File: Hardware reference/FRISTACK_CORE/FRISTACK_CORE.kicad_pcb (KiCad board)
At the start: 2 copper layers, 50 x 50 mm, 76 parts, among them J1 USB_C_Receptacle_USB2.0_16P, J3 Conn_01x04_Pin, J4 Conn_01x09_Socket, J5 Conn_01x12_Socket, J6 Conn_01x12_Socket, J7 Conn_01x04_Pin, J8 Conn_01x02_Pin, U1 AZ1117-3.3, U2 USBLC6-2SC6, U3 ESP32-S3-MINI-1U, U4 SN65HVD232, Y1 32.768 kHz

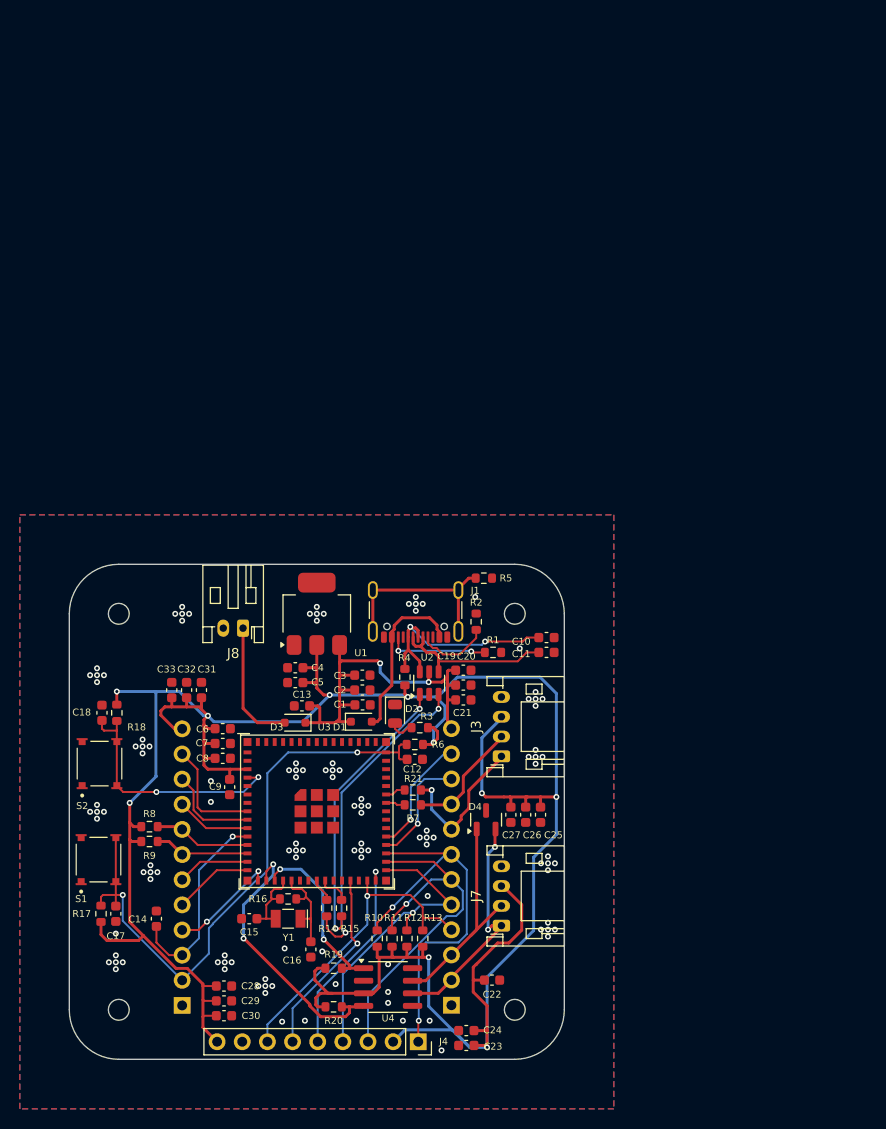
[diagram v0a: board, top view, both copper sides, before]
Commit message: Updated CORE schematic and PCB design
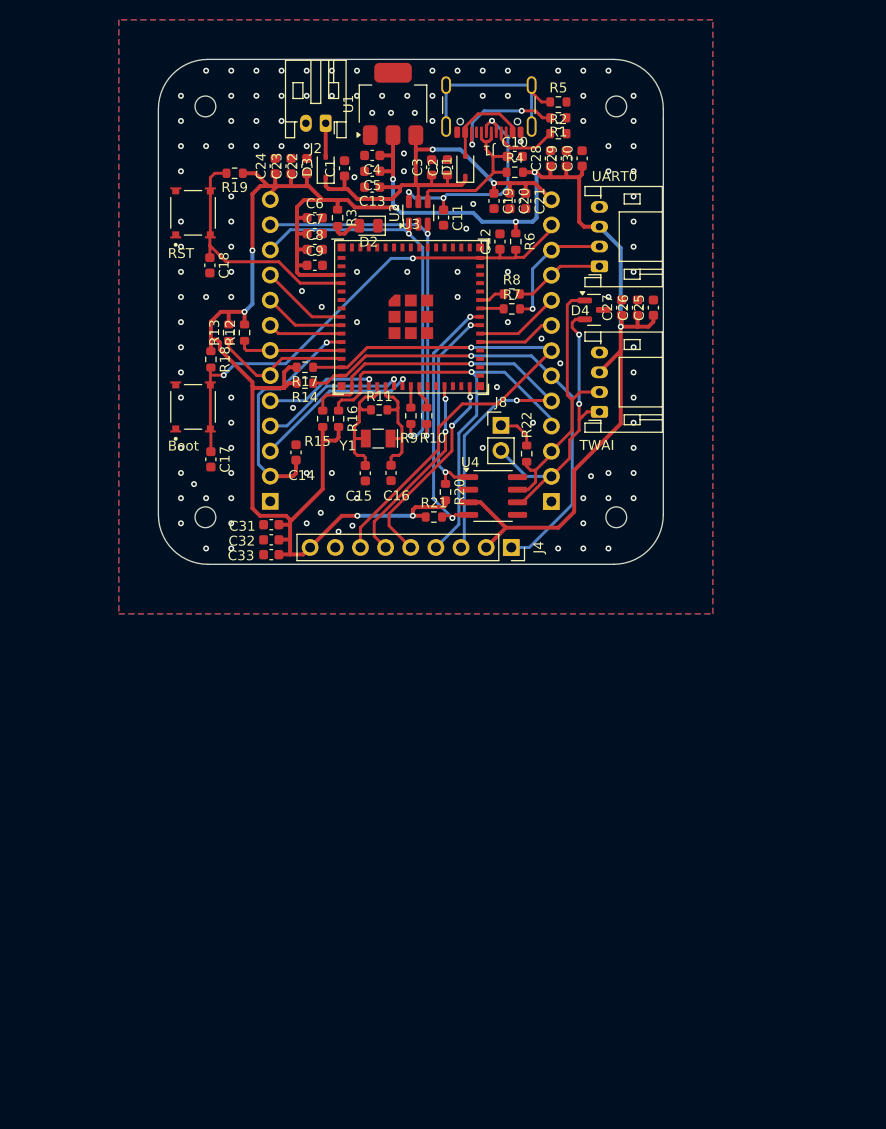
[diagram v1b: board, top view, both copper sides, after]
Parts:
- removed J3, J7: Conn_01x04_Pin, Connector_JST:JST_PH_S4B-PH-K_1x04_P2.00mm_Horizontal
- removed the REF** at (105.0, 105.0)
- removed the REF** at (105.0, 145.0)
- removed the REF** at (145.0, 145.0)
- removed the REF** at (145.0, 105.0)
- removed S1, S2: TL3315NF100Q, User_imports:SW_TL3315NF100Q
- added Boot: TL3315NF100Q, User_imports:SW_TL3315NF100Q, F.Cu at (112.5, 84.1)
- added J2: Conn_01x02_Pin, Connector_JST:JST_PH_S2B-PH-K_1x02_P2.00mm_Horizontal, F.Cu at (125.9, 55.5)
- added R22: 120, Resistor_SMD:R_0603_1608Metric, F.Cu at (146.2, 88.8)
- added REF**: MountingHole_2.1mm, MountingHole:MountingHole_2.1mm, F.Cu at (113.8, 95.2)
- added REF**: MountingHole_2.1mm, MountingHole:MountingHole_2.1mm, F.Cu at (155.2, 95.2)
- added REF**: MountingHole_2.1mm, MountingHole:MountingHole_2.1mm, F.Cu at (155.2, 53.8)
- added REF**: MountingHole_2.1mm, MountingHole:MountingHole_2.1mm, F.Cu at (113.8, 53.8)
- added RST: TL3315NF100Q, User_imports:SW_TL3315NF100Q, F.Cu at (112.5, 64.5)
- added TWAI: Conn_01x04_Pin, Connector_JST:JST_PH_S4B-PH-K_1x04_P2.00mm_Horizontal, F.Cu at (153.6, 84.6)
- added UART0: Conn_01x04_Pin, Connector_JST:JST_PH_S4B-PH-K_1x04_P2.00mm_Horizontal, F.Cu at (153.6, 69.9)
- J5, J6: value Conn_01x12_Socket -> Conn_01x13_Socket; footprint Connector_PinSocket_2.54mm:PinSocket_1x12_P2.54mm_Vertical -> Connector_PinSocket_2.54mm:PinSocket_1x13_P2.54mm_Vertical
- J8: footprint Connector_JST:JST_PH_S2B-PH-K_1x02_P2.00mm_Horizontal -> Connector_PinHeader_2.54mm:PinHeader_1x02_P2.54mm_Vertical
- R10: value 10K -> 0
- R11: value 10K -> ?
- R12, R13: value 10K -> 2K2
- R14, R15: value 0 -> 10K
- R16: value ? -> 10K
- R19: value 4K7 -> 10K
- R21: value 0 -> 4K7
- R8, R9: value 2K2 -> 0
- moved C30 93.9 mm to (151.8, 59.0), turned to 90 degrees
- moved C29 91.9 mm to (150.2, 59.0), turned to 90 degrees
- moved C23 90.6 mm to (122.4, 59.8), turned to 90 degrees
- moved C28 89.9 mm to (148.6, 59.0), turned to 90 degrees
- moved C24 89.4 mm to (120.8, 59.8), turned to 90 degrees
- moved C22 84.3 mm to (124.0, 59.8), turned to 90 degrees
- moved R19 80.9 mm to (116.7, 60.5)
- moved R8 65.1 mm to (144.7, 72.7), turned to 0 degrees
- moved R13 64.3 mm to (116.1, 76.6), turned to 90 degrees
- moved R12 63.4 mm to (117.7, 76.6), turned to 90 degrees
- moved R17 58.9 mm to (123.8, 80.1), turned to 180 degrees
- moved D1 57.1 mm to (140.0, 59.8), turned to 90 degrees
- moved D3 56.2 mm to (125.9, 59.9), turned to 90 degrees
- moved R1 54.4 mm to (149.4, 54.9)
- moved C1 54.2 mm to (127.8, 60.0), turned to 90 degrees
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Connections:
- J5 pad 10: I2S_DIN -> I2S_LRCK
- J5 pad 11: I2S_LRCK -> USB_DN_2
- J5 pad 12: ESP_PWR -> USB_DP_2
- J5 pad 2: EN -> ADC_1
- J5 pad 3: ADC_1 -> GPIO18
- J5 pad 4: GPIO12 -> GPIO17
- J5 pad 5: GPIO11 -> GPIO14
- J5 pad 6: GPIO10 -> SCL
- J5 pad 7: SCL -> SDA
- J5 pad 8: SDA -> I2S_DOUT
- J5 pad 9: I2S_DOUT -> I2S_DIN
- J6 pad 10: GPIO38 -> UART0_RX
- J6 pad 11: GPIO39 -> UART0_TX
- J6 pad 12: +5V -> EN
- J6 pad 4: CS -> MOSI
- J6 pad 5: MOSI -> SCK
- J6 pad 6: SCK -> MISO
- J6 pad 7: MISO -> CS
- J6 pad 8: UART0_RX -> GPIO39
- J6 pad 9: UART0_TX -> GPIO40
- J8 pad 1: Net-(D3-A) -> Net-(J8-Pin_1)
- J8 pad 2: GND -> CAN_L
- R10 pad 1: MISO -> Net-(U3-USB_D+)
- R10 pad 2: ESP_PWR -> USB_DP_2
- R11 pad 1: SCK -> X_TAL_N
- R11 pad 2: ESP_PWR -> X_TAL_P
- R12 pad 1: MOSI -> SDA
- R13 pad 1: CS -> SCL
- R14 pad 1: Net-(U3-USB_D-) -> MISO
- R14 pad 2: USB_DN_2 -> ESP_PWR
- R15 pad 1: Net-(U3-USB_D+) -> SCK
- R15 pad 2: USB_DP_2 -> ESP_PWR
- R16 pad 1: X_TAL_N -> MOSI
- R16 pad 2: X_TAL_P -> ESP_PWR
- R17 pad 1: ESP_PWR -> CS
- R17 pad 2: EN -> ESP_PWR
- R18 pad 2: GPIO0 -> EN
- R19 pad 1: CAN_D -> ESP_PWR
- R19 pad 2: ESP_PWR -> GPIO0
- R20 pad 1: ESP_PWR -> CAN_D
- R20 pad 2: CAN_R -> ESP_PWR
- R21 pad 1: Net-(U3-RXD0) -> ESP_PWR
- R21 pad 2: UART0_RX -> CAN_R
- R8 pad 1: SDA -> Net-(U3-RXD0)
- R8 pad 2: ESP_PWR -> UART0_RX
- R9 pad 1: SCL -> Net-(U3-USB_D-)
- R9 pad 2: ESP_PWR -> USB_DN_2
- U2 pad 1: USB_DP_2 -> USB_DN_2
- U2 pad 3: USB_DN_2 -> USB_DP_2
- U2 pad 4: USB_DN -> USB_DP
- U2 pad 6: USB_DP -> USB_DN
- U3 pad 14: GPIO10 -> CS
- U3 pad 15: GPIO11 -> MISO
- U3 pad 16: GPIO12 -> SCK
- U3 pad 17: CAN_R -> MOSI
- U3 pad 18: CAN_D -> GPIO14
- U3 pad 21: unconnected-(U3-IO17-Pad21) -> GPIO17
- U3 pad 22: unconnected-(U3-IO18-Pad22) -> GPIO18
- U3 pad 29: CS -> unconnected-(U3-IO34-Pad29)
- U3 pad 31: MOSI -> unconnected-(U3-IO35-Pad31)
- U3 pad 32: SCK -> unconnected-(U3-IO36-Pad32)
- U3 pad 33: MISO -> unconnected-(U3-IO37-Pad33)
- U3 pad 34: GPIO38 -> unconnected-(U3-IO38-Pad34)
- U3 pad 36: unconnected-(U3-IO40-Pad36) -> GPIO40
- U3 pad 37: unconnected-(U3-IO41-Pad37) -> CAN_D
- U3 pad 38: unconnected-(U3-IO42-Pad38) -> CAN_R
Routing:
- net ESP_PWR: track 277.8 -> 240.6 mm, vias 10 -> 9
- net CS: track 32.4 -> 55.1 mm
- net GPIO18: track 0.00 -> 17.2 mm, vias 0 -> 1
- net MOSI: track 30.8 -> 46.9 mm
- net GPIO17: track 0.00 -> 15.2 mm, vias 0 -> 1
- net SCK: track 37.6 -> 50.0 mm, vias 1 -> 2
- net GPIO14: track 0.00 -> 11.6 mm, vias 0 -> 1
- net GPIO38: track 11.6 -> 0.00 mm, vias 1 -> 0
- net EN: track 62.9 -> 51.3 mm
- net GPIO12: track 11.1 -> 0.00 mm, vias 2 -> 0
- net USB_DP_2: track 29.0 -> 38.8 mm
- net Net-(D3-A): track 13.2 -> 3.40 mm
- net GPIO40: track 0.00 -> 8.59 mm
- net GPIO11: track 8.05 -> 0.00 mm
- net CAN_L: track 24.3 -> 32.2 mm
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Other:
- board size 50 x 50 mm -> 51 x 51 mm
- board text removed: "+5V"
- board text removed: "ADC_1"
- board text removed: "CAN_H"
- board text removed: "CAN_L"
- board text removed: "CS"
- board text removed: "DC"
- board text removed: "EN"
- board text removed: "ESP_PWR"
- board text removed: "GND"
- board text removed: "GPIO10"
- board text removed: "GPIO11"
- board text removed: "GPIO12"
- board text removed: "GPIO38"
- board text removed: "GPIO39"
- board text removed: "I2S_DIN"
- board text removed: "I2S_DOUT"
- board text removed: "I2S_LRCK"
- board text removed: "MISO"
- board text removed: "MOSI"
- board text removed: "RST"
- board text removed: "SCK"
- board text removed: "SCL"
- board text removed: "SDA"
- board text removed: "UART0_RX"
- board text removed: "UART0_TX"

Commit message: Added SENSOR-NODE and reworked CORE
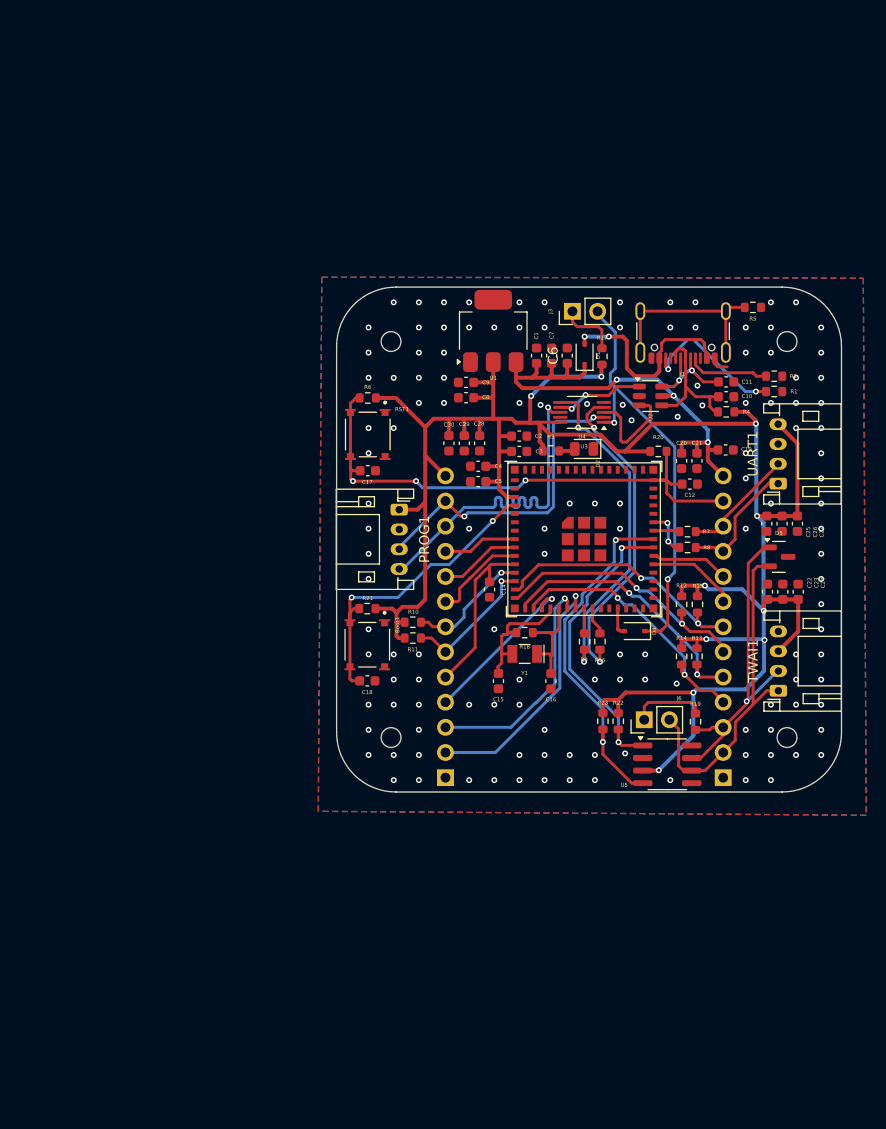
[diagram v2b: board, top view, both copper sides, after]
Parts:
- removed Boot, RST: TL3315NF100Q, User_imports:SW_TL3315NF100Q
- removed C13: 22uF, Capacitor_SMD:C_0603_1608Metric
- removed C31: 2.2uF, Capacitor_SMD:C_0603_1608Metric
- removed C32: 100nF, Capacitor_SMD:C_0603_1608Metric
- removed C33: 1nF, Capacitor_SMD:C_0603_1608Metric
- removed D3: 1N5819WS, Diode_SMD:D_SOD-323
- removed J2: Conn_01x02_Pin, Connector_JST:JST_PH_S2B-PH-K_1x02_P2.00mm_Horizontal
- removed J8: Conn_01x02_Pin, Connector_PinHeader_2.54mm:PinHeader_1x02_P2.54mm_Vertical
- removed the REF** at (113.8, 95.2)
- removed the REF** at (155.2, 95.2)
- removed the REF** at (155.2, 53.8)
- removed the REF** at (113.8, 53.8)
- removed TWAI, UART0: Conn_01x04_Pin, Connector_JST:JST_PH_S4B-PH-K_1x04_P2.00mm_Horizontal
- added Boot1: TL3315NF100Q, User_imports:SW_TL3315NF100Q, F.Cu at (130.1, 108.1)
- added D5: PESD1CAN, Package_TO_SOT_SMD:SOT-23, F.Cu at (171.7, 99.2)
- added G***: LOGO, User_imports:jano, B.Cu at (152.2, 97.6)
- added J3: Conn_01x02_Pin, Connector_PinHeader_2.54mm:PinHeader_1x02_P2.54mm_Vertical, F.Cu at (150.8, 74.5)
- added PROG1: Conn_01x04_Pin, Connector_JST:JST_PH_S4B-PH-K_1x04_P2.00mm_Horizontal, F.Cu at (133.3, 94.5)
- added R23: 4K7, Resistor_SMD:R_0603_1608Metric, F.Cu at (153.9, 115.8)
- added REF**: MountingHole_2mm, MountingHole:MountingHole_2mm, F.Cu at (132.5, 117.5)
- added REF**: MountingHole_2mm, MountingHole:MountingHole_2mm, F.Cu at (172.5, 117.5)
- added REF**: MountingHole_2mm, MountingHole:MountingHole_2mm, F.Cu at (132.5, 77.5)
- added REF**: MountingHole_2mm, MountingHole:MountingHole_2mm, F.Cu at (172.5, 77.5)
- added RST1: TL3315NF100Q, User_imports:SW_TL3315NF100Q, F.Cu at (130.2, 86.9)
- added TWAI1: Conn_01x04_Pin, Connector_JST:JST_PH_S4B-PH-K_1x04_P2.00mm_Horizontal, F.Cu at (171.6, 112.8)
- added U5: SN65HVD232, Package_SO:SOIC-8_3.9x4.9mm_P1.27mm, F.Cu at (160.4, 120.2)
- added UART1: Conn_01x04_Pin, Connector_JST:JST_PH_S4B-PH-K_1x04_P2.00mm_Horizontal, F.Cu at (171.6, 91.8)
- C2: value 10uF -> 22uF
- C3: value 0.1uF -> 100nF
- C4: value 0.1uF -> 1nF
- C5: value 10uF -> 100pF
- C6: value 22uF -> 10uF
- C7: value 100nF -> 0.1uF
- C8: value 1nF -> 0.1uF
- C9: value 100pF -> 10uF
- D4: value PESD1CAN -> 1N5819WS; footprint Package_TO_SOT_SMD:SOT-23 -> Diode_SMD:D_SOD-323
- J4: value Conn_01x09_Socket -> Conn_01x13_Socket; footprint Connector_PinSocket_2.54mm:PinSocket_1x09_P2.54mm_Vertical -> Connector_PinSocket_2.54mm:PinSocket_1x13_P2.54mm_Vertical; moved to B.Cu
- J6: value Conn_01x13_Socket -> Conn_01x02_Pin; footprint Connector_PinSocket_2.54mm:PinSocket_1x13_P2.54mm_Vertical -> Connector_PinHeader_2.54mm:PinHeader_1x02_P2.54mm_Vertical; moved to F.Cu
- R10: value 0 -> 4K7
- R11: value ? -> 4K7
- R12, R13: value 2K2 -> 10K
- R16: value 10K -> 22
- R18: value 10K -> ?
- R19: value 10K -> 120
- R20, R21: value 4K7 -> 10K
- R22: value 120 -> 4K7
- R7: value 499 -> 22
- R8, R9: value 0 -> 22
- U4: value SN65HVD232 -> FUSB42; footprint Package_SO:SOIC-8_3.9x4.9mm_P1.27mm -> Package_SO:VSSOP-10_3x3mm_P0.5mm
- moved R19 72.4 mm to (163.2, 115.9), turned to 90 degrees
- moved C24 68.1 mm to (173.6, 102.8)
- moved C23 65.7 mm to (172.1, 102.8)
- moved C22 63.4 mm to (170.5, 102.8)
- moved R13 57.5 mm to (163.4, 109.3)
- moved J5 53.6 mm to (166.1, 121.5)
- moved R12 52.0 mm to (161.8, 104.0)
- moved R14 47.0 mm to (161.8, 109.3), turned to 90 degrees
- moved C18 44.9 mm to (130.1, 111.8), turned to 0 degrees
- moved R15 42.2 mm to (163.4, 104.0), turned to 90 degrees
- moved R18 42.0 mm to (146.0, 106.9), turned to 180 degrees
- moved R1 35.2 mm to (171.2, 82.5)
- moved R16 34.7 mm to (153.6, 107.8)
- moved C19 34.4 mm to (166.3, 88.5), turned to 0 degrees
- moved C4 33.2 mm to (141.3, 90.1)
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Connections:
- net USB_DN renamed USB_N
- net USB_DP renamed USB_P
- C2 pad 1: +5V -> ESP_PWR
- C3 pad 1: +5V -> ESP_PWR
- C6 pad 1: ESP_PWR -> +5V
- C7 pad 1: ESP_PWR -> +5V
- D4 pad 1: CAN_H -> Net-(D4-K)
- D4 pad 2: CAN_L -> GPIO47
- J4 pad 1: MISO -> GND
- J4 pad 2: ESP_PWR -> GPIO18
- J4 pad 3: SCK -> GPIO17
- J4 pad 4: MOSI -> GPIO14
- J4 pad 5: DC -> ADC_1
- J4 pad 6: RST_LCD -> SCL
- J4 pad 7: CS -> SDA
- J4 pad 8: GND -> I2S_DOUT
- J4 pad 9: ESP_PWR -> I2S_DIN
- J5 pad 10: I2S_LRCK -> UART0_RX
- J5 pad 11: USB_DN_2 -> UART0_TX
- J5 pad 12: USB_DP_2 -> EN
- J5 pad 13: ESP_PWR -> +5V
- J5 pad 2: ADC_1 -> CAN_L
- J5 pad 3: GPIO18 -> CAN_H
- J5 pad 4: GPIO17 -> MOSI
- J5 pad 5: GPIO14 -> SCK
- J5 pad 6: SCL -> MISO
- J5 pad 7: SDA -> CS
- J5 pad 8: I2S_DOUT -> GPIO39
- J5 pad 9: I2S_DIN -> GPIO40
- J6 pad 1: GND -> Net-(J6-Pin_1)
- R10 pad 1: Net-(U3-USB_D+) -> SDA
- R10 pad 2: USB_DP_2 -> ESP_PWR
- R11 pad 1: X_TAL_N -> SCL
- R11 pad 2: X_TAL_P -> ESP_PWR
- R12 pad 1: SDA -> MISO
- R13 pad 1: SCL -> SCK
- R14 pad 1: MISO -> MOSI
- R15 pad 1: SCK -> CS
- R16 pad 1: MOSI -> Net-(U3-USB_D+)
- R16 pad 2: ESP_PWR -> USB_P_ESP
- R17 pad 1: CS -> ESP_PWR
- R17 pad 2: ESP_PWR -> Net-(J3-Pin_1)
- R18 pad 1: ESP_PWR -> X_TAL_N
- R18 pad 2: EN -> X_TAL_P
- R19 pad 1: ESP_PWR -> CAN_H
- R19 pad 2: GPIO0 -> Net-(J6-Pin_1)
- R20 pad 1: CAN_D -> ESP_PWR
- R20 pad 2: ESP_PWR -> EN
- R21 pad 2: CAN_R -> GPIO0
- R22 pad 1: CAN_H -> CAN_D
- R22 pad 2: Net-(J8-Pin_1) -> ESP_PWR
- R9 pad 2: USB_DN_2 -> USB_N_ESP
- U2 pad 1: USB_DN_2 -> USB_N_2
- U2 pad 3: USB_DP_2 -> USB_P_2
- U3 pad 27: RST_LCD -> GPIO47
- U3 pad 30: DC -> unconnected-(U3-IO48-Pad30)
- U4 pad 1: CAN_D -> Net-(D4-K)
- U4 pad 2: GND -> USB_N_HD
- U4 pad 3: ESP_PWR -> USB_P_2
- U4 pad 4: CAN_R -> USB_P_ESP
- U4 pad 5: unconnected-(U4-NC-Pad5) -> GND
- U4 pad 6: CAN_L -> USB_N_ESP
- U4 pad 7: CAN_H -> USB_N_2
- U4 pad 8: unconnected-(U4-NC-Pad8) -> USB_P_HD
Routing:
- net Net-(D4-K): track 0.00 -> 42.9 mm, vias 0 -> 2
- net USB_DN_2: track 38.9 -> 0.00 mm, vias 2 -> 0
- net USB_DP_2: track 38.8 -> 0.00 mm, vias 2 -> 0
- net USB_P_HD: track 0.00 -> 34.8 mm, vias 0 -> 1
- net USB_N_ESP: track 0.00 -> 33.5 mm, vias 0 -> 2
- net USB_P_ESP: track 0.00 -> 32.8 mm, vias 0 -> 2
- net USB_N_HD: track 0.00 -> 32.7 mm, vias 0 -> 2
- net CS: track 55.1 -> 26.2 mm, vias 1 -> 2
- net SCK: track 50.0 -> 27.7 mm
- net DC: track 21.2 -> 0.00 mm, vias 2 -> 0
- net MISO: track 47.9 -> 27.1 mm, vias 1 -> 2
- net RST_LCD: track 19.9 -> 0.00 mm, vias 2 -> 0
- net MOSI: track 46.9 -> 27.3 mm, vias 1 -> 2
- net USB_N: track 23.0 -> 10.5 mm, vias 3 -> 2
- net Net-(D1-A): track 9.40 -> 21.6 mm, vias 0 -> 2
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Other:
- outline, holes or cut-outs redrawn
